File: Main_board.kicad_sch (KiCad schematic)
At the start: 90 parts, among them J1 USB_C_Receptacle, SW100 SW_Push, SW101 SW_Push, SW102 SW_Push, SW103 SW_Push, SW104 SW_Push, SW105 SW_Push, SW21 SW_Push, SW22 SW_Push, SW23 SW_Push, SW24 SW_Push, SW25 SW_Push, SW26 SW_Push, SW27 SW_Push, SW28 SW_Push, SW29 SW_Push, SW30 SW_Push, SW31 SW_Push, SW32 SW_Push, SW33 SW_Push, SW34 SW_Push, SW35 SW_Push, SW36 SW_Push, SW37 SW_Push, SW38 SW_Push, SW39 SW_Push, SW40 SW_Push, SW41 SW_Push, SW42 SW_Push, SW43 SW_Push, SW44 SW_Push, SW45 SW_Push, SW46 SW_Push, SW47 SW_Push, SW48 SW_Push, SW49 SW_Push, SW50 SW_Push, SW51 SW_Push, SW52 SW_Push, SW53 SW_Push, SW54 SW_Push, SW55 SW_Push, SW56 SW_Push, SW57 SW_Push, SW58 SW_Push, SW59 SW_Push, SW60 SW_Push, SW61 SW_Push, SW62 SW_Push, SW63 SW_Push, SW64 SW_Push, SW65 SW_Push, SW66 SW_Push, SW67 SW_Push, SW68 SW_Push, SW69 SW_Push, SW70 SW_Push, SW71 SW_Push, SW72 SW_Push, SW73 SW_Push, SW74 SW_Push, SW75 SW_Push, SW76 SW_Push, SW77 SW_Push, SW78 SW_Push, SW79 SW_Push, SW80 SW_Push, SW81 SW_Push, SW82 SW_Push, SW83 SW_Push, SW84 SW_Push, SW85 SW_Push, SW86 SW_Push, SW87 SW_Push, SW88 SW_Push, SW89 SW_Push, SW90 SW_Push, SW91 SW_Push, SW92 SW_Push, SW93 SW_Push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

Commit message: Schematic checkpoint before I mess up the layout
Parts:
- removed J1: USB_C_Receptacle, symbol Connector:USB_C_Receptacle
- removed U4: MDBT50Q-1MV2, MDBT50Q-1MV2:XCVR_MDBT50Q-1MV2, symbol MDBT50Q-1MV2:MDBT50Q-1MV2
- added C1, C2: 4.7µf, Capacitor_SMD:C_0805_2012Metric, symbol Device:C
- added C3: 1µF, Capacitor_SMD:C_0805_2012Metric, symbol Device:C
- added C4: 2.2µF, Capacitor_SMD:C_0805_2012Metric, symbol Device:C
- added C5, C6, C7, C8: 10µF, Capacitor_SMD:C_0805_2012Metric, symbol Device:C
- added Conn1, Conn3, Conn4: Conn_01x06_Pin, Connector_PinHeader_2.54mm:PinHeader_1x06_P2.54mm_Vertical, symbol Connector:Conn_01x06_Pin
- added Conn2: Conn_01x06_Pin, Connector_PinSocket_2.54mm:PinSocket_1x06_P2.54mm_Vertical, symbol Connector:Conn_01x06_Pin
- added D100, D101, D102, D103, D104, D105, D21, D22, D23, D24, D25, D26, D27, D28, D29, D30, D31, D32, D33, D34, D35, D36, D37, D38, D39, D40, D41, D42, D43, D44, D45, D46, D47, D48, D49, D50, D51, D52, D53, D54, D55, D56, D57, D58, D59, D60, D61, D62, D63, D64, D65, D66, D67, D68, D69, D70, D71, D72, D73, D74, D75, D76, D77, D78, D79, D80, D81, D82, D83, D84, D85, D86, D87, D88, D89, D90, D91, D92, D93, D94, D95, D96, D97, D98, D99: D, Diode_SMD:D_SOD-123, symbol Device:D
- added D106: ESDA5V3L, Package_TO_SOT_SMD:SOT-23-3, symbol Power_Protection:ESDA5V3L
- added J1: USB_C_Receptacle_USB2.0_14P, Connector_USB:USB_C_Receptacle_HRO_TYPE-C-31-M-12, symbol Connector:USB_C_Receptacle_USB2.0_14P
- added J3: Conn_02x03_Odd_Even, Connector_PinHeader_1.00mm:PinHeader_2x03_P1.00mm_Vertical, symbol Connector_Generic:Conn_02x03_Odd_Even
- added R10: 2kΩ, Resistor_SMD:R_0805_2012Metric, symbol Device:R
- added R11, R12: 27R, Resistor_SMD:R_0805_2012Metric, symbol Device:R
- added R13: 80.6kΩ, Resistor_SMD:R_0805_2012Metric, symbol Device:R
- added R14: 100kΩ, Resistor_SMD:R_0805_2012Metric, symbol Device:R
- added R15: 34.8kΩ, Resistor_SMD:R_0805_2012Metric, symbol Device:R
- added R16: 10kΩ, Resistor_SMD:R_0805_2012Metric, symbol Device:R
- added R17, R18: 4.7kΩ, Resistor_SMD:R_0805_2012Metric, symbol Device:R
- added R8: 806kΩ, Resistor_SMD:R_0805_2012Metric, symbol Device:R
- added R9: 2MΩ, Resistor_SMD:R_0805_2012Metric, symbol Device:R
- added TP3: BAT, TestPoint:TestPoint_Pad_D2.0mm, symbol Connector:TestPoint
- added TP4: GND, TestPoint:TestPoint_Pad_D2.0mm, symbol Connector:TestPoint
- added U4: MCP73831-4-OT, Package_TO_SOT_SMD:SOT-23-5, symbol Battery_Management:MCP73831-4-OT
- added U5: LP2985-3.3, Package_TO_SOT_SMD:SOT-23-5, symbol Regulator_Linear:LP2985-3.3
- added U6: USB6B1, Package_SO:SOIC-8_3.9x4.9mm_P1.27mm, symbol Power_Protection:USB6B1
- added U7: LTC4217, LTC4217IDHC_PBF:DFN-16_DHC, symbol Custom Symbols:LTC4217
- R6, R7: footprint (none) -> Resistor_SMD:R_0805_2012Metric
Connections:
- net GND: now also R6.2, R7.2, C1.2, C2.2, C3.2, C4.2, C5.2, C6.2, C7.2, C8.2, Conn1.6 (Pin_6), Conn2.6 (Pin_6), Conn3.6 (Pin_6), Conn4.6 (Pin_6), D106.3 (A), J1.A1 (GND), J1.A12 (GND), J1.B1 (GND), J1.B12 (GND), J1.S1 (SHIELD), J3.3 (Pin_3), J3.6 (Pin_6), R10.2, R14.1, R16.2, R9.1, TP4.1, U4.2 (V_{SS}), U5.2 (GND), U6.4 (GND), U6.5 (GND), U7.6,17 (GND)
- net M3V3: now also C4.1, J3.1 (Pin_1), R17.1, R18.1, U5.5 (VOUT); no longer U3.28 (VDD)
- net MCOL0: now also U3.3 (P1.10)
- net MCOL1: now also U3.4 (P1.11)
- net MCOL10: now also U3.13 (P0.28)
- net MCOL11: now also U3.14 (P0.30)
- net MCOL12: now also U3.16 (P0.27)
- net MCOL13: now also U3.17 (P0.00)
- net MCOL14: now also U3.18 (P0.01)
- net MCOL2: now also U3.5 (P1.12)
- net MCOL3: now also U3.6 (P1.13)
- net MCOL4: now also U3.7 (P1.14)
- net MCOL5: now also U3.8 (P1.15)
- net MCOL6: now also U3.9 (P0.03)
- net MCOL7: now also U3.10 (P0.29)
- net MCOL8: now also U3.11 (P0.02)
- net MCOL9: now also U3.12 (P0.31)
- net MROW0: now also D21.1 (K), D22.1 (K), D23.1 (K), D24.1 (K), D25.1 (K), D26.1 (K), D27.1 (K), D28.1 (K), D29.1 (K), D30.1 (K), D31.1 (K), D32.1 (K), D33.1 (K), D34.1 (K); no longer SW21.2, SW22.2, SW23.2, SW24.2, SW25.2, SW26.2, SW27.2, SW28.2, SW29.2, SW30.2, SW31.2, SW32.2, SW33.2, SW34.2
- net MROW1: now also D35.1 (K), D36.1 (K), D37.1 (K), D38.1 (K), D39.1 (K), D40.1 (K), D41.1 (K), D42.1 (K), D43.1 (K), D44.1 (K), D45.1 (K), D46.1 (K), D47.1 (K), D48.1 (K), D49.1 (K); no longer SW35.2, SW36.2, SW37.2, SW38.2, SW39.2, SW40.2, SW41.2, SW42.2, SW43.2, SW44.2, SW45.2, SW46.2, SW47.2, SW48.2, SW49.2
- net MROW2: now also D50.1 (K), D51.1 (K), D52.1 (K), D53.1 (K), D54.1 (K), D55.1 (K), D56.1 (K), D57.1 (K), D58.1 (K), D59.1 (K), D60.1 (K), D61.1 (K), D62.1 (K), D63.1 (K), D64.1 (K); no longer SW50.2, SW51.2, SW52.2, SW53.2, SW54.2, SW55.2, SW56.2, SW57.2, SW58.2, SW59.2, SW60.2, SW61.2, SW62.2, SW63.2, SW64.2
- net MROW3: now also D65.1 (K), D66.1 (K), D67.1 (K), D68.1 (K), D69.1 (K), D70.1 (K), D71.1 (K), D72.1 (K), D73.1 (K), D74.1 (K), D75.1 (K), D76.1 (K), D77.1 (K), D78.1 (K), D79.1 (K); no longer SW65.2, SW66.2, SW67.2, SW68.2, SW69.2, SW70.2, SW71.2, SW72.2, SW73.2, SW74.2, SW75.2, SW76.2, SW77.2, SW78.2, SW79.2
- net MROW4: now also D80.1 (K), D81.1 (K), D82.1 (K), D83.1 (K), D84.1 (K), D85.1 (K), D86.1 (K), D87.1 (K), D88.1 (K), D89.1 (K), D90.1 (K), D91.1 (K), D92.1 (K), D93.1 (K); no longer SW80.2, SW81.2, SW82.2, SW83.2, SW84.2, SW85.2, SW86.2, SW87.2, SW88.2, SW89.2, SW90.2, SW91.2, SW92.2, SW93.2
- net MROW5: now also D100.1 (K), D101.1 (K), D102.1 (K), D103.1 (K), D104.1 (K), D105.1 (K), D94.1 (K), D95.1 (K), D96.1 (K), D97.1 (K), D98.1 (K), D99.1 (K); no longer SW100.2, SW101.2, SW102.2, SW103.2, SW104.2, SW105.2, SW94.2, SW95.2, SW96.2, SW97.2, SW98.2, SW99.2
- net MSCL: now also U3.47 (P1.00), Conn1.2 (Pin_2), Conn2.2 (Pin_2), Conn3.2 (Pin_2), Conn4.2 (Pin_2), D106.1 (K), R17.2; no longer U3.23 (P0.07)
- net MSDA: now also U3.26 (P1.09), Conn1.3 (Pin_3), Conn2.3 (Pin_3), Conn3.3 (Pin_3), Conn4.3 (Pin_3), D106.2 (K), R18.2; no longer U3.22 (P0.06)
- net MVBUS: now also U3.30 (VDDH), C1.1, C7.1, J1.A4 (VBUS), J1.A9 (VBUS), J1.B4 (VBUS), J1.B9 (VBUS), R13.2, R15.1, U4.4 (V_{DD}), U6.1 (VBUS), U6.8 (VBUS), U7.1,16 (VDD)
- net at R6.1: now also J1.A5 (CC1)
- net at R7.1: now also J1.B5 (CC2)
- net MINT4: now reaches U3.25 (P1.08)
- net MRESET: now reaches U3.40 (P0.18)
- net MRESET: now also J3.5 (Pin_5)
- net MID2: now reaches U3.50 (P1.02)
- net MID2: now also Conn2.5 (Pin_5)
- net MSWDIO: now reaches U3.51 (SWDIO)
- net MSWDIO: now also J3.2 (Pin_2)
- net MSWDCLK: now reaches U3.53 (SWDCLK)
- net MSWDCLK: now also J3.4 (Pin_4)
- net MBT_PIN: now reaches U3.54 (P0.10)
- net MBT_PIN: now also R8.1, R9.2
- net MID4: now reaches U3.56 (P1.04)
- net MID4: now also Conn3.5 (Pin_5)
- net MINT2: now reaches U3.57 (P1.06)
- net MINT2: now also Conn2.4 (Pin_4)
- net MINT3: now reaches U3.58 (P1.07)
- net MINT3: now also Conn3.4 (Pin_4)
- net MINT1: now reaches U3.59 (P1.05)
- net MINT1: now also Conn1.4 (Pin_4)
- net MID3: now reaches U3.60 (P1.03)
- net MID1: now reaches U3.61 (P1.01)
- net MID1: now also Conn1.5 (Pin_5)
- net D+: no longer names the net of U3.35 (D+)
- net D+: now also R12.1
- net D-: no longer names the net of U3.34 (D-)
- net D-: now also R11.2
- net MCOM renamed MUSB_DET
- net MUSB_DET: now also R13.1, R14.2
- net MPRESENCE renamed MFLT
- net MFLT: now also U7.12 (FLT)
- new net: D46.2 (A), SW46.2
- new net: D59.2 (A), SW59.2
- new net: D58.2 (A), SW58.2
- new net: D37.2 (A), SW37.2
- new net: D73.2 (A), SW73.2
- new net: D35.2 (A), SW35.2
- new net: D28.2 (A), SW28.2
- new net: D102.2 (A), SW102.2
- new net: D98.2 (A), SW98.2
- new net: D62.2 (A), SW62.2
- new net: D77.2 (A), SW77.2
- new net: D81.2 (A), SW81.2
- new net: D85.2 (A), SW85.2
- new net: D93.2 (A), SW93.2
- new net: D49.2 (A), SW49.2
- new net: D76.2 (A), SW76.2
- new net: D103.2 (A), SW103.2
- new net: D61.2 (A), SW61.2
- new net: D87.2 (A), SW87.2
- new net: R15.2, R16.1, U7.3 (OV)
- new net: D44.2 (A), SW44.2
- new net: D31.2 (A), SW31.2
- new net: D64.2 (A), SW64.2
- new net: D105.2 (A), SW105.2
- new net: D69.2 (A), SW69.2
- new net: D47.2 (A), SW47.2
- new net: D99.2 (A), SW99.2
- new net: D88.2 (A), SW88.2
- new net: D68.2 (A), SW68.2
- new net: D104.2 (A), SW104.2
- new net: D57.2 (A), SW57.2
- new net: D53.2 (A), SW53.2
- new net: D38.2 (A), SW38.2
- new net: D51.2 (A), SW51.2
- new net: D23.2 (A), SW23.2
- new net: D95.2 (A), SW95.2
- new net: D75.2 (A), SW75.2
- new net: D33.2 (A), SW33.2
- new net: D70.2 (A), SW70.2
- new net: C5.1, U5.4 (BP)
- new net: D26.2 (A), SW26.2
- new net: D21.2 (A), SW21.2
- new net: D92.2 (A), SW92.2
- new net: D82.2 (A), SW82.2
- new net: C8.1, U7.4 (TIMER), U7.5 (INTV_CC)
- new net: D66.2 (A), SW66.2
- new net: D65.2 (A), SW65.2
- new net: D97.2 (A), SW97.2
- new net: D22.2 (A), SW22.2
- new net: D94.2 (A), SW94.2
- new net: D52.2 (A), SW52.2
- new net: D84.2 (A), SW84.2
- new net: D40.2 (A), SW40.2
- new net: D63.2 (A), SW63.2
- new net: D72.2 (A), SW72.2
- new net: D32.2 (A), SW32.2
- new net: D90.2 (A), SW90.2
- new net: D67.2 (A), SW67.2
- new net: D48.2 (A), SW48.2
- new net: D54.2 (A), SW54.2
- new net: D50.2 (A), SW50.2
- new net: D74.2 (A), SW74.2
- new net: D41.2 (A), SW41.2
- new net: D89.2 (A), SW89.2
- new net: D27.2 (A), SW27.2
- new net: D45.2 (A), SW45.2
- new net: D43.2 (A), SW43.2
- new net: D34.2 (A), SW34.2
- new net: R10.1, U4.5 (PROG)
- new net: D86.2 (A), SW86.2
- new net: D29.2 (A), SW29.2
- new net: D80.2 (A), SW80.2
- new net: D101.2 (A), SW101.2
- new net: D71.2 (A), SW71.2
- new net: D39.2 (A), SW39.2
- new net: D79.2 (A), SW79.2
- new net: D91.2 (A), SW91.2
- new net: D100.2 (A), SW100.2
- new net: D25.2 (A), SW25.2
- new net: D96.2 (A), SW96.2
- new net: J1.A7 (D-), J1.B7 (D-), U6.2 (I/O1)
- new net: J1.A6 (D+), J1.B6 (D+), U6.3 (I/O2)
- new net: D36.2 (A), SW36.2
- new net: D60.2 (A), SW60.2
- new net: D56.2 (A), SW56.2
- new net: D78.2 (A), SW78.2
- new net: D83.2 (A), SW83.2
- new net: D30.2 (A), SW30.2
- new net: D55.2 (A), SW55.2
- new net: D42.2 (A), SW42.2
- new net: C6.1, U3.28 (VDD)
- new net: D24.2 (A), SW24.2
- new net MD+: R12.2, U6.6 (I/O2)
- new net MD-: R11.1, U6.7 (I/O1)
- new net MID6: Conn4.5 (Pin_5)
- new net MINT5: Conn4.4 (Pin_4)
- new net MVBAT: C2.1, C3.1, R8.2, TP3.1, U4.3 (V_{BAT}), U5.1 (VIN), U5.3 (ON/~{OFF})
- new net MVBUS_SW: Conn1.1 (Pin_1), Conn2.1 (Pin_1), Conn3.1 (Pin_1), Conn4.1 (Pin_1), U7.13 (FB), U7.7,8,9 (OUT)
- new net MVB_EN: U3.22 (P0.06), U7.2 (UV)
- no-connect marks 0 -> 11
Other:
- moved on the sheet: R6, R7, SW100, SW101, SW102, SW103, SW104, SW105, SW21, SW22, SW23, SW24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

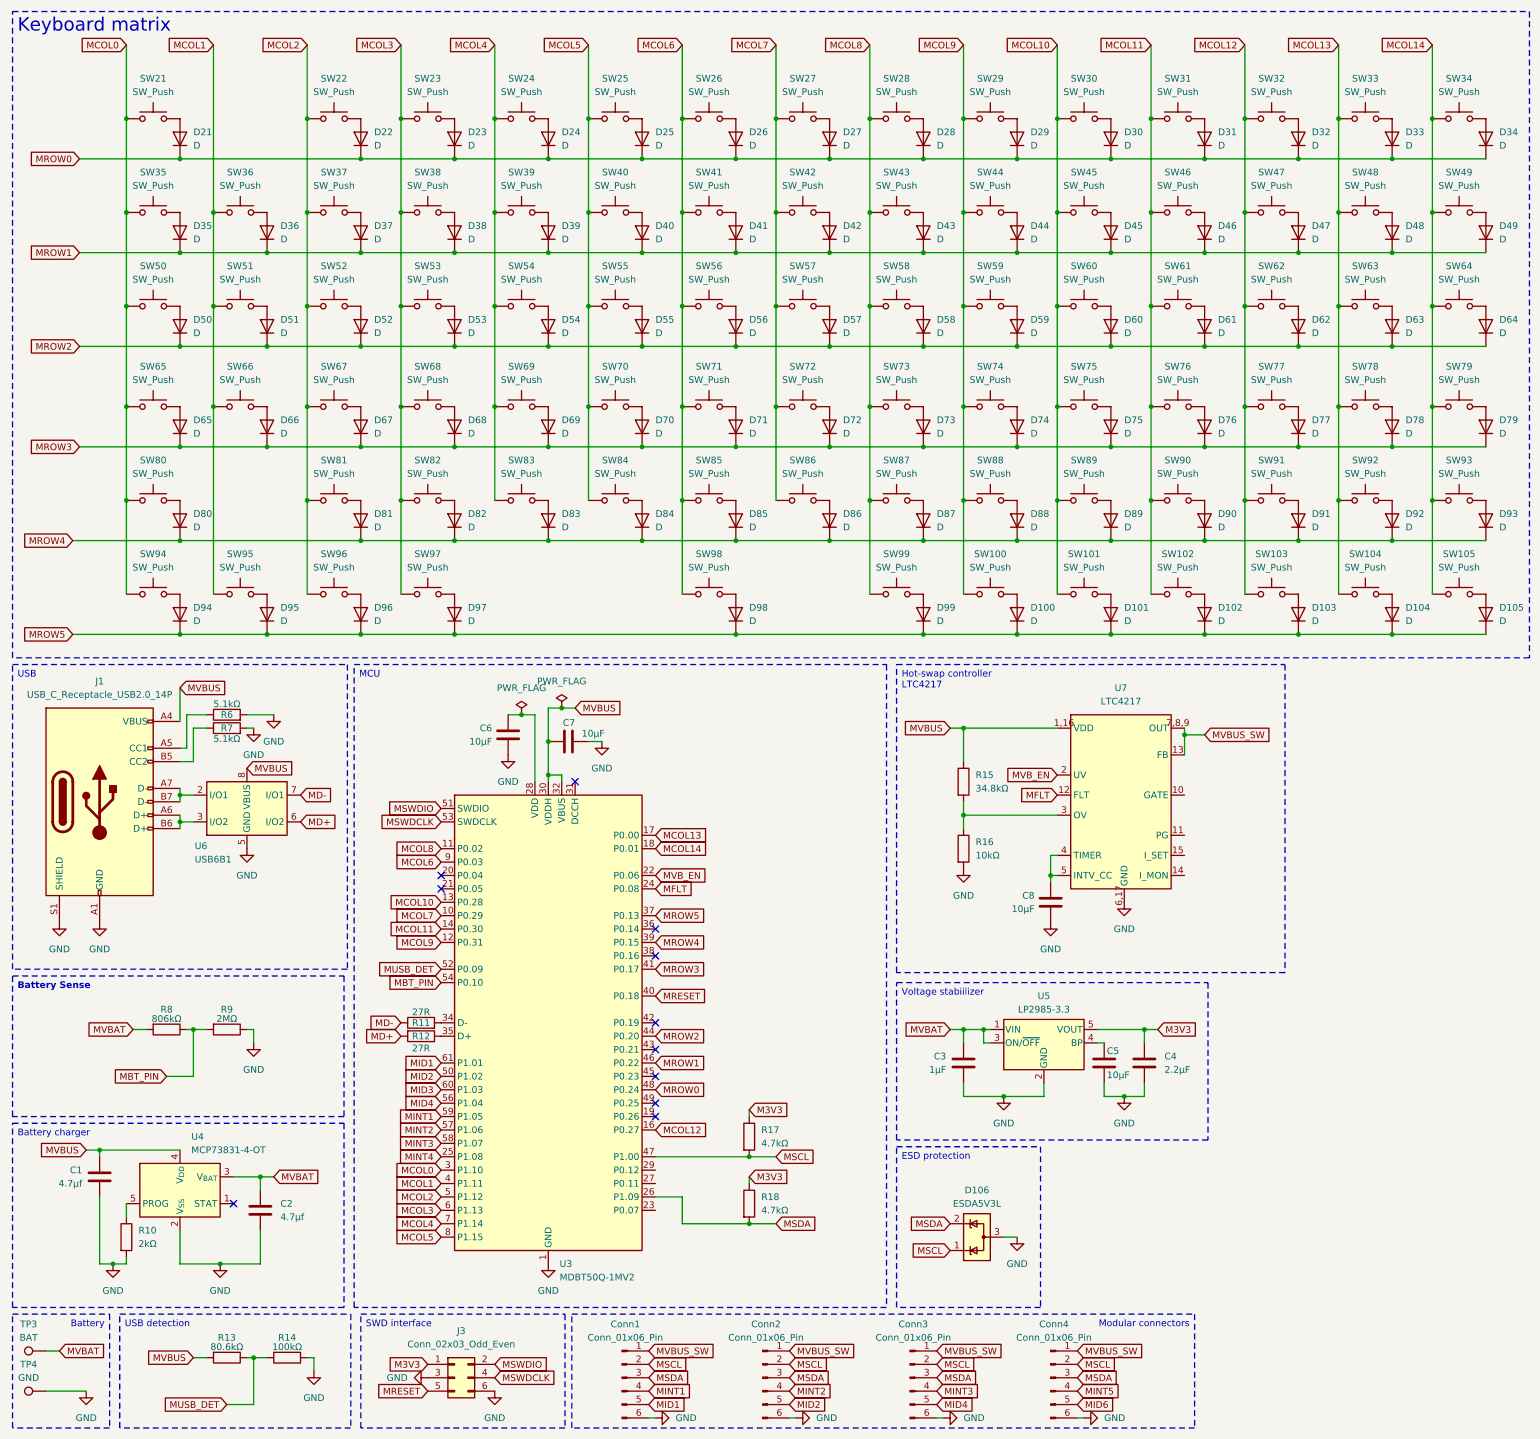
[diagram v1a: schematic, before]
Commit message: I gave up on the hotswao modularity thing
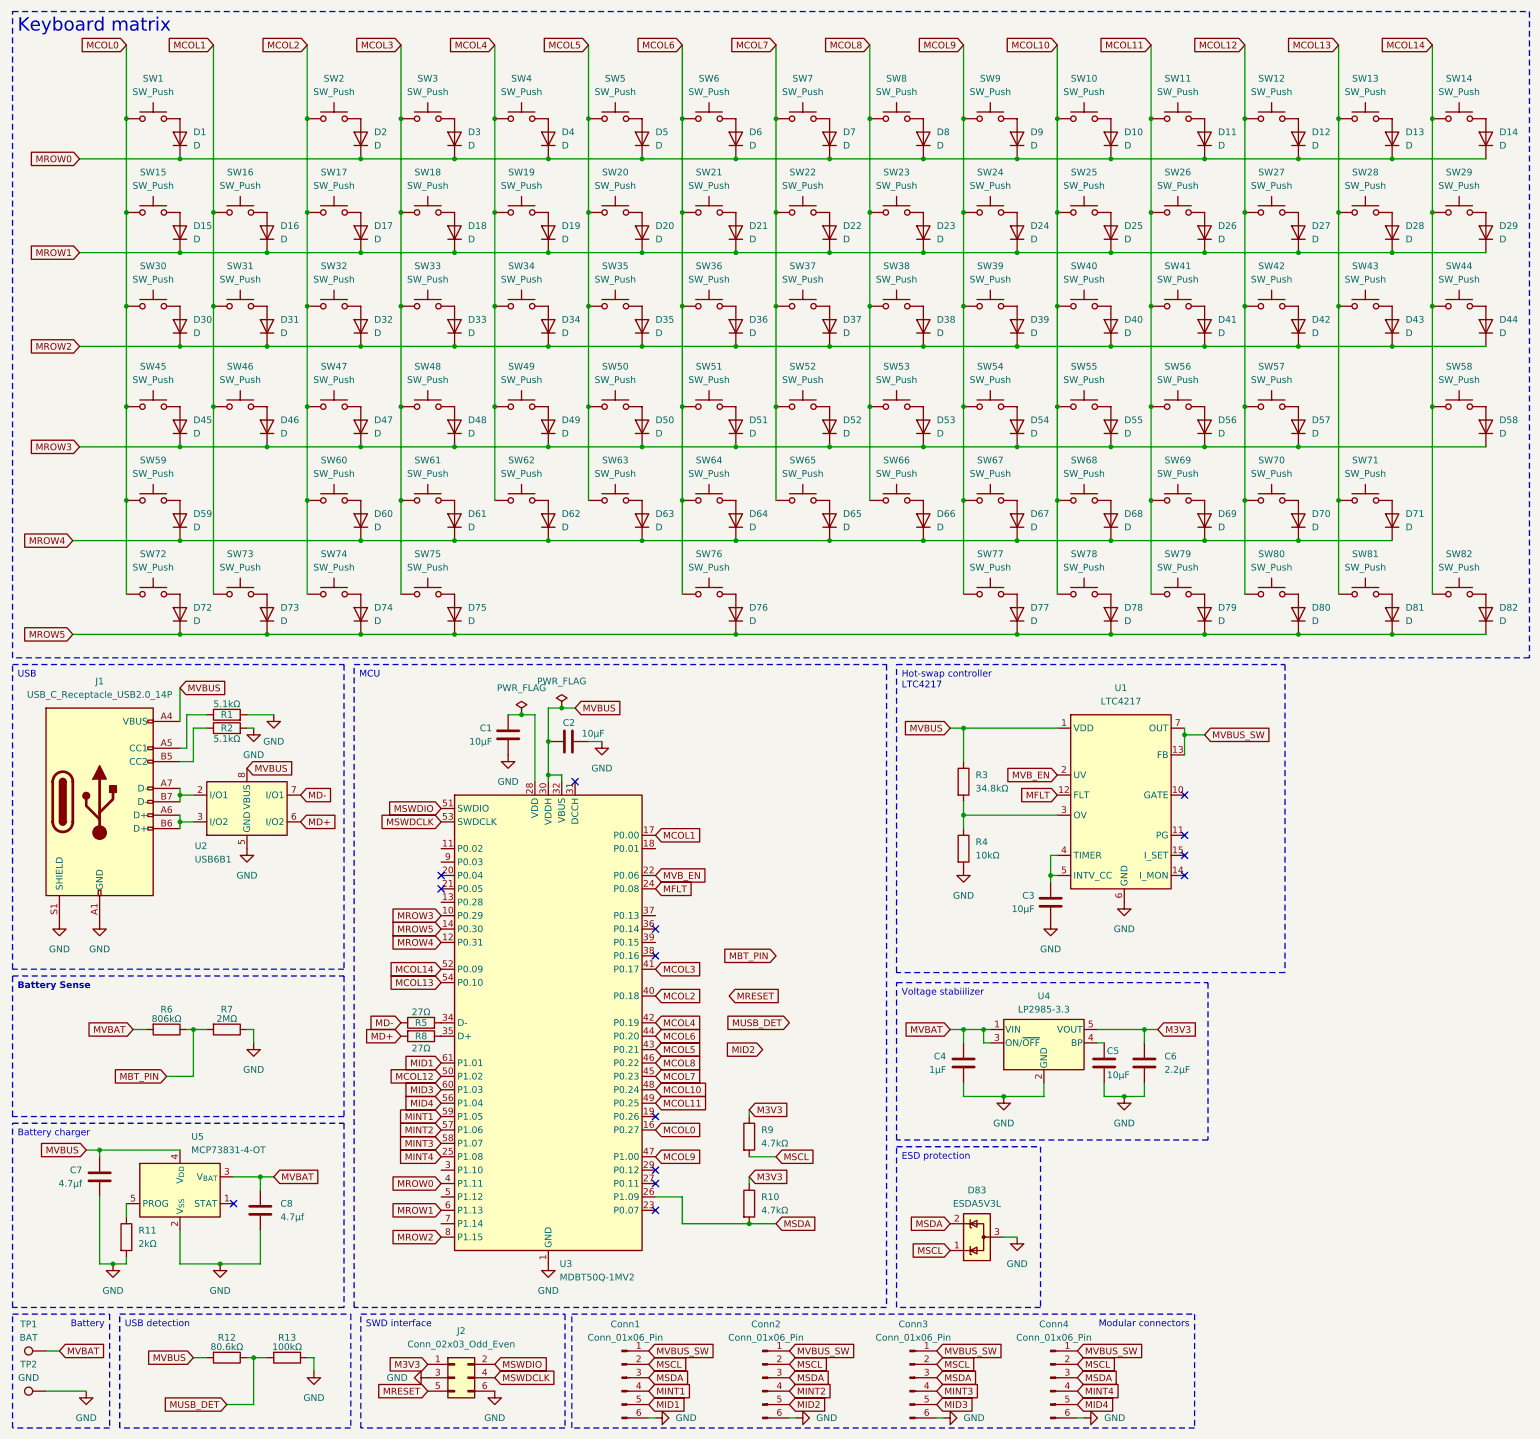
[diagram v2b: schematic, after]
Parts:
- removed D105, D77, D91: D, Diode_SMD:D_SOD-123, symbol Device:D
- removed SW105, SW77, SW91: SW_Push, PCM_marbastlib-choc:SW_choc_v1_HS_CPG135001S30_1u, symbol Switch:SW_Push
- R5: renamed from R11; value 27R -> 27Ω
- R8: renamed from R12; value 27R -> 27Ω
- renumbered C6 to C1, C7 to C2, C8 to C3, C3 to C4, C4 to C6, C1 to C7, C2 to C8, D21 to D1, D30 to D10, D31 to D11, D32 to D12, D33 to D13, D34 to D14, D35 to D15, D36 to D16, D37 to D17, D38 to D18, D39 to D19, D22 to D2, D40 to D20, D41 to D21, D42 to D22, D43 to D23, D44 to D24, D45 to D25, D46 to D26, D47 to D27, D48 to D28, D49 to D29, D23 to D3, D50 to D30, D51 to D31, D52 to D32, D53 to D33, D54 to D34, D55 to D35, D56 to D36, D57 to D37, D58 to D38, D59 to D39, D24 to D4, D60 to D40, D61 to D41, D62 to D42, D63 to D43, D64 to D44, D65 to D45, D66 to D46, D67 to D47, D68 to D48, D69 to D49, D25 to D5, D70 to D50, D71 to D51, D72 to D52, D73 to D53, D74 to D54, D75 to D55, D76 to D56, D78 to D57, D79 to D58, D80 to D59, D26 to D6, D81 to D60, D82 to D61, D83 to D62, D84 to D63, D85 to D64, D86 to D65, D87 to D66, D88 to D67, D89 to D68, D90 to D69, D27 to D7, D92 to D70, D93 to D71, D94 to D72, D95 to D73, D96 to D74, D97 to D75, D98 to D76, D99 to D77, D100 to D78, D101 to D79, D28 to D8, D102 to D80, D103 to D81, D104 to D82, D106 to D83, D29 to D9, J3 to J2, R6 to R1, R18 to R10, R10 to R11, R13 to R12, R14 to R13, R7 to R2, R15 to R3, R16 to R4, R8 to R6, R9 to R7, R17 to R9, SW21 to SW1, SW30 to SW10, SW31 to SW11, SW32 to SW12, SW33 to SW13, SW34 to SW14, SW35 to SW15, SW36 to SW16, SW37 to SW17, SW38 to SW18, SW39 to SW19, SW22 to SW2, SW40 to SW20, SW41 to SW21, SW42 to SW22, SW43 to SW23, SW44 to SW24, SW45 to SW25, SW46 to SW26, SW47 to SW27, SW48 to SW28, SW49 to SW29, SW23 to SW3, SW50 to SW30, SW51 to SW31, SW52 to SW32, SW53 to SW33, SW54 to SW34, SW55 to SW35, SW56 to SW36, SW57 to SW37, SW58 to SW38, SW59 to SW39, SW24 to SW4, SW60 to SW40, SW61 to SW41, SW62 to SW42, SW63 to SW43, SW64 to SW44, SW65 to SW45, SW66 to SW46, SW67 to SW47, SW68 to SW48, SW69 to SW49, SW25 to SW5, SW70 to SW50, SW71 to SW51, SW72 to SW52, SW73 to SW53, SW74 to SW54, SW75 to SW55, SW76 to SW56, SW78 to SW57, SW79 to SW58, SW80 to SW59, SW26 to SW6, SW81 to SW60, SW82 to SW61, SW83 to SW62, SW84 to SW63, SW85 to SW64, SW86 to SW65, SW87 to SW66, SW88 to SW67, SW89 to SW68, SW90 to SW69, SW27 to SW7, SW92 to SW70, SW93 to SW71, SW94 to SW72, SW95 to SW73, SW96 to SW74, SW97 to SW75, SW98 to SW76, SW99 to SW77, SW100 to SW78, SW101 to SW79, SW28 to SW8, SW102 to SW80, SW103 to SW81, SW104 to SW82, SW29 to SW9, TP3 to TP1, TP4 to TP2, U7 to U1, U6 to U2, U5 to U4, U4 to U5
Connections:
- net MID6 is gone; now on net MID4: Conn4.5 (Pin_5)
- net MINT5 is gone; now on net MINT4: Conn4.4 (Pin_4)
- net GND: now also U1.17 (GND), U1.6 (GND); no longer U1.6,17 (GND)
- net MBT_PIN: no longer U3.54 (P0.10)
- net MCOL0: now also U3.16 (P0.27); no longer U3.3 (P1.10)
- net MCOL1: now also U3.17 (P0.00); no longer U3.4 (P1.11)
- net MCOL10: now also SW78.1, U3.48 (P0.24); no longer SW79.1, U3.13 (P0.28)
- net MCOL11: now also SW79.1, U3.49 (P0.25); no longer SW80.1, U3.14 (P0.30)
- net MCOL12: now also SW57.1, SW70.1, SW80.1, U3.50 (P1.02); no longer SW81.1, U3.16 (P0.27)
- net MCOL13: now also SW71.1, SW81.1, U3.54 (P0.10); no longer SW57.1, SW70.1, SW82.1, U3.17 (P0.00)
- net MCOL14: now also SW82.1, U3.52 (P0.09); no longer SW71.1, U3.18 (P0.01)
- net MCOL2: now also U3.40 (P0.18); no longer U3.5 (P1.12)
- net MCOL3: now also U3.41 (P0.17); no longer U3.6 (P1.13)
- net MCOL4: now also U3.42 (P0.19); no longer U3.7 (P1.14)
- net MCOL5: now also U3.43 (P0.21); no longer U3.8 (P1.15)
- net MCOL6: now also U3.44 (P0.20); no longer U3.9 (P0.03)
- net MCOL7: now also U3.45 (P0.23); no longer U3.10 (P0.29)
- net MCOL8: now also U3.46 (P0.22); no longer SW77.1, U3.11 (P0.02)
- net MCOL9: now also SW77.1, U3.47 (P1.00); no longer SW78.1, U3.12 (P0.31)
- net MID2: no longer U3.50 (P1.02)
- net MID3: now also Conn3.5 (Pin_5)
- net MID4: no longer Conn3.5 (Pin_5)
- net MRESET: no longer U3.40 (P0.18)
- net MROW0: now also U3.4 (P1.11); no longer U3.48 (P0.24)
- net MROW1: now also U3.6 (P1.13); no longer U3.46 (P0.22)
- net MROW2: now also U3.8 (P1.15); no longer U3.44 (P0.20)
- net MROW3: now also U3.10 (P0.29); no longer U3.41 (P0.17)
- net MROW4: now also U3.12 (P0.31); no longer U3.39 (P0.15)
- net MROW5: now also U3.14 (P0.30); no longer U3.37 (P0.13)
- net MSCL: no longer U3.47 (P1.00)
- net MUSB_DET: no longer U3.52 (P0.09)
- net MVBUS_SW: now also U1.7 (OUT), U1.8 (OUT), U1.9 (OUT); no longer U1.7,8,9 (OUT)
- net MVBUS renamed VDD
- net VDD: now also U1.1 (VDD), U1.16 (VDD); no longer U1.1,16 (VDD)
- no-connect marks 11 -> 14
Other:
- moved on the sheet: D57, D70, D71, D77, D78, D79, D80, D81, D82, SW57, SW70, SW71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
